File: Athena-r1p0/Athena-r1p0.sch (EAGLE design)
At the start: 86 parts, among them J1 MF-CON-MICROUSB-RIGHT, J3 TC2050-IDC-NL, J4 TC2030-IDC-NL, J5 MF-CON-2.54mm-01x14, J6 MF-CON-2.54mm-01x14, SW1 MF-SW-TACT-4.2MM, SW2 MF-SW-TACT-4.2MM, U1 AP2112, U2 RT9080-18GJ5, U3 MCP73831/2, U4 PRTR5V0U2X,215, U5 FE310, U6 32MBit, U7 MK22FN128VLH10, X1 JST 2-Pin, Y1 TSX-3225-16.0000MF18X-AC0, Y2 KX3211A0032.768000

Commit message: Finished updates based on design review feedback.  Added mounting holes and chassis GND.  Converted all passives to 0402.  Renumbered all parts.  Added cover page.  Replaced SiTime oscillator with std footprint 32kHz oscillator.
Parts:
- removed C33, C34: 15pF, MF_Passives:CAPACITOR_NP_0603
- removed C35, C36, C37: 0.1uF, MF_Passives:CAPACITOR_NP_0402
- removed TP1, TP2, TP3, TP4: TEST-POINT3X5, Athena-r0p1:TEST-POINT3X5
- added B0, B1, B2, B3: TPB0,65, Athena-r0p1:TPB0,65
- added C23, C25: 10uF, MF_Passives:CAPACITOR_NP_0402
- added C24, C26, C29: 0.1uF, MF_Passives:CAPACITOR_NP_0402
- added J7, J8: MF-CON-2.54mm-01x06, MF_Connectors:CON_01X06_PTH_2.54MM
- added MGT1, MGT2, MGT3, MGT4: MOUNTING_HOLE, Athena-r0p1:MOUNTING_HOLE
- added R22, R23: 10, MF_Passives:RESISTOR_0402
- C1, C12: device MF_Passives:CAPACITOR_NP_0603 -> MF_Passives:CAPACITOR_NP_0402; MPN (none) -> CL05A106MP8NUB8
- C10, C20: value 10nF -> 0.1uF; device MF_Passives:CAPACITOR_NP_0603 -> MF_Passives:CAPACITOR_NP_0402
- C11, C16, C18: device MF_Passives:CAPACITOR_NP_0603 -> MF_Passives:CAPACITOR_NP_0402
- C13, C22: value 10uF -> 0.1uF
- C14: value 10uF -> DNP
- C15: value 10uF -> 0.01uF
- C17: value DNP -> 10uF; device MF_Passives:CAPACITOR_NP_0603 -> MF_Passives:CAPACITOR_NP_0402; MPN (none) -> CL05A106MP8NUB8
- C19: value 0.1uF -> 10uF; device MF_Passives:CAPACITOR_NP_0603 -> MF_Passives:CAPACITOR_NP_0402; MPN (none) -> CL05A106MP8NUB8
- C21: MPN (none) -> CL05A106MP8NUB8
- C27: value 0.1uF -> 10uF; MPN (none) -> CL05A106MP8NUB8
- C28: value 0.1uF -> 0.01uF
- C3: value 1uF -> 10uF; MPN (none) -> CL05A106MP8NUB8
- C30: value 0.1uF -> 15pF; MPN (none) -> CL05C150JB5NNNC
- C31: value 10uF -> 15pF; device MF_Passives:CAPACITOR_NP_0603 -> MF_Passives:CAPACITOR_NP_0402; MPN (none) -> CL05C150JB5NNNC
- C6: value 10uF -> 1uF; device MF_Passives:CAPACITOR_NP_0603 -> MF_Passives:CAPACITOR_NP_0402
- D1: value MF-LED-0603-GREEN -> MF-LED-0603-RED; device MF_LEDs:LED_SINGLE-0603-GREEN -> MF_LEDs:LED_SINGLE-0603-RED
- D2: value MF-LED-0603-RED -> MF-LED-0603-GREEN; device MF_LEDs:LED_SINGLE-0603-RED -> MF_LEDs:LED_SINGLE-0603-GREEN
- FRAME1: SHEETNM Power (Nest) -> Power
- FRAME2: SHEETNM USB-JTAG (NEST) -> MK22 Controller (Nest)
- FRAME3: SHEETNM OFF-BOARD-DEBUG HEADER -> Bridge and Debug Headers
- FRAME4: SHEETNM Microcontroller (Owl) -> FE310 Microcontroller (Owl)
- FRAME6: SHEETNM Headers (Owl) -> I/O Headers (Owl)
- J2: value (none) -> G800LS588010THR
- J5, J6: value MF-CON-2.54mm-01x14 -> MF-CON-2.54mm-01x08; device MF_Connectors:CON_01X14_PTH_2.54MM -> MF_Connectors:CON_01X08_PTH_2.54MM
- R1: value 100k -> 1k
- R10, R11, R12, R9: value 100k -> 100; device MF_Passives:RESISTOR_0603 -> MF_Passives:RESISTOR_0402
- R13, R14: value 100 -> 100k
- R15: value 100 -> 0
- R16: value 100k -> 1M
- R17: value 1M -> 100k; device MF_Passives:RESISTOR_0603 -> MF_Passives:RESISTOR_0402
- R18: value DNP -> 100k
- R2: value 100k -> 10k
- R20: value 100k -> 10
- R21: value 0 -> 10
- R3, R5: value 1k -> 100k
- R4: value 100k -> 1k; device MF_Passives:RESISTOR_0603 -> MF_Passives:RESISTOR_0402
- R6: value 10k -> DNP
- R8: value 100 -> 100k; device MF_Passives:RESISTOR_0603 -> MF_Passives:RESISTOR_0402
- U1: value AP2112 -> PRTR5V0U2X,215; device Athena-r0p1:AP2112 -> Athena-r0p1:PRTR5V0U2X,215
- U2: value RT9080-18GJ5 -> MCP73831/2; device Athena-r0p1:RT9080-18GJ5 -> Athena-r0p1:MCP73831/2
- U3: value MCP73831/2 -> AP2112; device Athena-r0p1:IC_POWER_LIPO_MCP73831/2 -> Athena-r0p1:AP2112
- U4: value PRTR5V0U2X,215 -> RT9080-18GJ5; device Athena-r0p1:PRTR5V0U2X,215 -> Athena-r0p1:RT9080-18GJ5
- U5: value FE310 -> MK22FN128VLH10; device Athena-r0p1:IC_MCU_SIFIVE_FE310 -> Athena-r0p1:MK22FN128VLH10
- U6: value 32MBit -> FE310; device Athena-r0p1:IC_MEMORY_QSPI32MBIT -> Athena-r0p1:IC_MCU_SIFIVE_FE310
- U7: value MK22FN128VLH10 -> 32MBit; device Athena-r0p1:IC_USB_JTAG_MK22FN128VLH10 -> Athena-r0p1:IC_MEMORY_QSPI32MBIT
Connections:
- removed net BATT_VOLT: J6.PIN4, R19.P$2, R20.P$1
- removed net CS2: J5.PIN8, U5.IO9
- removed net CS3: J5.PIN9, U5.IO10
- removed net IO22: J6.PIN10, U5.IO22
- removed net P35: TP1.1, U7.PTB0/LLWU_P5
- removed net P36: TP2.1, U7.PTB1
- removed net P37: TP3.1, U7.PTB2
- removed net P38: TP4.1, U7.PTB3
- removed net PWM0_0: J6.PIN5, U5.IO0
- removed net PWM0_1: J6.PIN6, U5.IO1
- removed net VOLT_BAT: C1.P$2, C10.P$2, C11.P$2, C12.P$2, C13.P$2, C14.P$2, C15.P$2, C18.P$2, C19.P$2, C2.P$2, C20.P$2, C21.P$2, C22.P$2, C27.P$2, C28.P$2, C3.P$2, C30.P$2, C31.P$2, C32.P$2, C33.P$2, C34.P$2, C35.P$2, C36.P$2, C37.P$2, C4.P$2, C5.P$2, C6.P$2, C7.P$2, C8.P$2, C9.P$2, D4.A, D5.A, J1.GND, J1.SLD, J2.15, J2.16, J3.10, J3.7, J3.8, J3.9, J4.5, R18.P$1, R20.P$2, R21.P$2, R3.P$2, R6.P$1, SW1.P$1, SW1.P$2, SW2.P$1, SW2.P$2, U1.GND, U2.GND, U3.VSS, U4.GND/1, U5.GND, U6.GND, U7.GND, U7.VREFL, U7.VSSA, X1.2, Y1.2, Y1.4, Y2.GND
- new net CGND: J1.SLD, MGT1.P$1, MGT2.P$1, MGT3.P$1, MGT4.P$1, R20.P$1, R21.P$1, R22.P$1, R23.P$1
- new net IO1: J6.PIN2, U6.IO1
- new net IO10: J7.PIN2, U6.IO10
- new net IO9: J7.PIN1, U6.IO9
- new net N$12: B0.TP, U5.PTB0/LLWU_P5
- new net N$13: B1.TP, U5.PTB1
- new net N$14: B2.TP, U5.PTB2
- new net N$15: B3.TP, U5.PTB3
- new net PWM: J6.PIN1, U6.IO0
- net 1.8V: now also C15.P$1, C16.P$1, C17.P$1, C6.P$1, J8.PIN3, R12.P$1, U4.VOUT, U6.VDD_CORE; no longer C10.P$1, C11.P$1, C12.P$1, C5.P$1, R8.P$1, U2.VOUT, U5.VDD_CORE
- net 16MHZ_IN: now also C30.P$1, R16.P$1, U6.XTAL_IN; no longer C33.P$1, R17.P$2, U5.XTAL_IN
- net 16MHZ_OUT: now also C31.P$1, R16.P$2, U6.XTAL_OUT; no longer C34.P$1, R17.P$1, U5.XTAL_OUT
- net 3.3V: now also C10.P$1, C11.P$1, C12.P$1, C20.P$1, C23.P$1, C24.P$1, C25.P$1, C26.P$1, C29.P$1, C5.P$1, D2.ANODE, J5.PIN7, J8.PIN2, R13.P$1, R14.P$1, R17.P$1, R18.P$1, R19.P$1, R6.P$2, R8.P$1, U3.OUT, U4.VIN, U5.PTA4/LLWU_P3, U5.USBVDD, U5.VBATT, U5.VDD, U5.VDDA, U5.VREFH, U6.AON_VDD, U6.AON_VDD_IO, U6.OTP_AIVDD, U6.VDD_IO, U7.VCC; no longer C13.P$1, C14.P$1, C15.P$1, C28.P$1, C3.P$1, C30.P$1, C31.P$1, C35.P$1, C36.P$1, C37.P$1, D1.ANODE, J5.PIN14, J5.PIN2, J6.PIN14, R10.P$1, R11.P$1, R12.P$1, R16.P$1, R4.P$1, R7.P$2, R9.P$1, U1.OUT, U2.VIN, U5.AON_VDD, U5.AON_VDD_IO, U5.OTP_AIVDD, U5.VDD_IO, U6.VCC, U7.PTA4/LLWU_P3, U7.USBVDD, U7.VBATT, U7.VDD, U7.VDDA, U7.VREFH
- net 32KHZ_CLK: now also U6.AON_PSD_LFALTCLK; no longer U5.AON_PSD_LFALTCLK
- net CS0: now also J5.PIN3, U6.IO2; no longer J5.PIN4, U5.IO2
- net DBG_RESET: now also R8.P$2, U5.RESET_B; no longer R16.P$2, U7.RESET_B
- net DBG_SWDCLK: now also U5.PTA0; no longer U7.PTA0
- net DBG_SWDIO: now also U5.PTA3; no longer U7.PTA3
- net DBG_SWO: now also U5.PTA2; no longer U7.PTA2
- net GND: now also C1.P$2, C10.P$2, C11.P$2, C12.P$2, C15.P$2, C16.P$2, C17.P$2, C18.P$2, C19.P$2, C2.P$2, C20.P$2, C21.P$2, C22.P$2, C23.P$2, C24.P$2, C25.P$2, C26.P$2, C27.P$2, C28.P$2, C29.P$2, C3.P$2, C30.P$2, C31.P$2, C32.P$2, C4.P$2, C5.P$2, C6.P$2, C7.P$2, C8.P$2, C9.P$2, D4.A, D5.A, J1.GND, J2.15, J2.16, J3.10, J3.7, J3.8, J3.9, J4.5, J5.PIN8, J6.PIN8, J8.PIN5, J8.PIN6, R15.P$2, R2.P$1, R20.P$2, R21.P$2, R22.P$2, R23.P$2, R4.P$2, R7.P$1, SW1.P$1, SW1.P$2, SW2.P$1, SW2.P$2, U1.GND/1, U2.VSS, U3.GND, U4.GND, U5.GND, U5.VREFL, U5.VSSA, U6.GND, U7.GND, X1.2, Y1.2, Y1.4, Y2.GND; no longer J5.PIN13, J5.PIN3, J6.PIN13
- net IO11: now also J7.PIN3, U6.IO11; no longer J5.PIN10, U5.IO11
- net IO19: now also J7.PIN4, U6.IO19; no longer J6.PIN7, U5.IO19
- net IO20: now also J7.PIN5, U6.IO20; no longer J6.PIN8, U5.IO20
- net IO21: now also J7.PIN6, U6.IO21; no longer J6.PIN9, U5.IO21
- net JTAG_TCK: now also U6.JTAG_TCK; no longer U5.JTAG_TCK
- net JTAG_TCK_NEST: now also R10.P$2; no longer R14.P$2
- net JTAG_TDI: now also U6.JTAG_TDI; no longer U5.JTAG_TDI
- net JTAG_TDI_NEST: now also R9.P$2; no longer R13.P$2
- net JTAG_TDO: now also U6.JTAG_TDO; no longer U5.JTAG_TDO
- net JTAG_TDO_NEST: now also U5.PTE1/LLWU_P0; no longer U7.PTE1/LLWU_P0
- net JTAG_TMS: now also U6.JTAG_TMS; no longer U5.JTAG_TMS
- net JTAG_TMS_NEST: now also R11.P$1; no longer R15.P$1
- net MISO: now also J5.PIN5, U6.IO4; no longer J5.PIN6, U5.IO4
- net MOSI: now also J5.PIN6, U6.IO3; no longer J5.PIN5, U5.IO3
- net N$1: now also R3.P$1, U3.EN; no longer R1.P$1, U1.EN
- net N$10: now also C13.P$2, C14.P$2, U6.PLL_AVSS; no longer C16.P$2, C17.P$2, U5.PLL_AVSS
- net N$11: now also R9.P$1, U5.PTD2/LLWU_P13; no longer R15.P$2, U7.PTD6/LLWU_P15
- net N$2: now also D2.CATHODE, R4.P$1; no longer D1.CATHODE, R3.P$1
- net N$3: now also D1.CATHODE, R1.P$1; no longer D2.CATHODE, R5.P$1
- net N$4: now also R5.P$2, R6.P$1, R7.P$2, U4.EN; no longer R18.P$2, R2.P$2, R7.P$1, U2.EN
- net N$5: now also R2.P$2, U2.PROG; no longer R6.P$2, U3.PROG
- net N$6: now also R1.P$2, U2.STAT; no longer R5.P$2, U3.STAT
- net N$7: now also R15.P$1, U6.AON_PSD_LFCLKSEL; no longer R21.P$1, U5.AON_PSD_LFCLKSEL
- net N$8: now also R11.P$2, U5.PTD6/LLWU_P15; no longer R13.P$1, U7.PTD2/LLWU_P13
- net N$9: now also R10.P$1, U5.PTD5; no longer R14.P$1, U7.PTD5
- net PLL_AVDD: now also C13.P$1, C14.P$1, R12.P$2, U6.PLL_AVDD; no longer C16.P$1, C17.P$1, R8.P$2, U5.PLL_AVDD
- net QSPI_CS: now also R19.P$2, U6.QSPI_CS, U7.CE#; no longer R10.P$2, U5.QSPI_CS, U6.CE#
- net QSPI_DQ0: now also U6.QSPI_DQ_0, U7.MOSI/IO0; no longer U5.QSPI_DQ_0, U6.MOSI/IO0
- net QSPI_DQ1: now also U6.QSPI_DQ_1, U7.MISO/IO1; no longer U5.QSPI_DQ_1, U6.MISO/IO1
- net QSPI_DQ2: now also R17.P$2, U6.QSPI_DQ_2, U7.WP#/IO2; no longer R4.P$2, U5.QSPI_DQ_2, U6.WP#/IO2
- net QSPI_DQ3: now also R18.P$2, U6.QSPI_DQ_3, U7.HOLD#/IO3; no longer R9.P$2, U5.QSPI_DQ_3, U6.HOLD#/IO3
- net QSPI_SCK: now also U6.QSPI_SCK, U7.SCK; no longer U5.QSPI_SCK, U6.SCK
- net RESET: now also C28.P$1, J5.PIN2, R14.P$2, U6.AON_ERST_N; no longer C20.P$1, J6.PIN1, R12.P$2, U5.AON_ERST_N
- net RESET_NEST: now also U5.PTD7; no longer U7.PTD7
- net RXI: now also J6.PIN3, U6.IO23; no longer J6.PIN12, U5.IO23
- net SCK: now also J5.PIN4, U6.IO5; no longer J5.PIN7, U5.IO5
- net SCL: now also J6.PIN5, U6.IO13; no longer J5.PIN12, U5.IO13
- net SDA: now also J6.PIN6, U6.IO12; no longer J5.PIN11, U5.IO12
- net TXO: now also J6.PIN4, U6.IO18; no longer J6.PIN11, U5.IO18
- net UART_RX: now also U6.IO16; no longer U5.IO16
- net UART_RX_NEST: now also U5.PTB16; no longer U7.PTB16
- net UART_TX: now also U6.IO17; no longer U5.IO17
- net UART_TX_NEST: now also U5.PTB17; no longer U7.PTB17
- net USB_N: now also U1.3, U5.D-; no longer U4.3, U7.D-
- net USB_P: now also U1.2, U5.D+; no longer U4.2, U7.D+
- net VDD_CORE_EN: now also J8.PIN4, R5.P$1, U6.AON_PMU_OUT_0; no longer J6.PIN3, R2.P$1, U5.AON_PMU_OUT_0
- net V_BATT: now also C1.P$1, U2.VBAT; no longer C6.P$1, R19.P$1, U3.VBAT
- net V_USB: now also C3.P$1, D1.ANODE, J6.PIN7, J8.PIN1, R3.P$2, U1.VDD/4, U2.VDD, U3.IN; no longer C1.P$1, D2.ANODE, J5.PIN1, R1.P$2, U1.IN, U3.VDD, U4.VDD/4
- net WAKE: now also J5.PIN1, R13.P$2, U6.AON_DWAKEUP_N; no longer J6.PIN2, R11.P$2, U5.AON_DWAKEUP_N
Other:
- note added: "1"
- note added: "2"
- note added: "3"
- note added: "4"
- note added: "5"
- note added: "6"
- note added: "7"
- note added: "Athena Design Rev. 1.0 Schematic"
- note added: "Aug. 5, 2021"
- note added: "Cover Page"
- note added: "Debug Control: MK22 Processor"
- note added: "Debug Headers: MK22 Tag, FE310 Tag, MK22->FE310 Bridge"
- note added: "Description"
- note added: "Designed in EAGLE 9.6.2."
- note added: "GPIO Header"
- note added: "I/O Headers: mikroBus-Compatible, GPIO, and Power; Mechanical"
- note added: "J2 Bridge connector notes Default: Closed (1->2, 3->4, ..., 15->16) to program/debug on-board (Athena) FE310. Open and access NEST-side pins to program/debug off-board FE310 using Athena MK22 controller."
- note added: "Main Processor: SiFive FE310, the RISC-V MCU"
- note added: "Mechanical & Grounds"
- note added: "Peripherals: Oscillators, Flash Memory"
- note added: "Power Header"
- note added: "Power: USB, Charging, Voltage Regulators"
- note added: "RVR Lab, Rice University, Houston TX"
- note added: "Sheet"
- note added: "The first RISC-V development board at Rice University, featuring the SiFive FE310 microprocessor, Athena is a prototyping and experimental platform for education and research at Rice. It is intended to be used in undergraduate lab courses and in VIP projects, therefore the design focus is on debug capability and I/O access."
- note added: "mikroBus Left Header"
- note added: "mikroBus Right Header"
- note removed: "CONTROL"
- note removed: "GPIO"
- note removed: "I2C"
- note removed: "J1 Bridge connector notes Default: Closed (1->2, 3->4, ..., 15->16) to program/debug on-board (Athena) FE310. Open and access NEST-side pins to program/debug off-board FE310 using Athena MK22 controller."
- note removed: "POWER"
- note removed: "SPI1"
- note removed: "UART1"

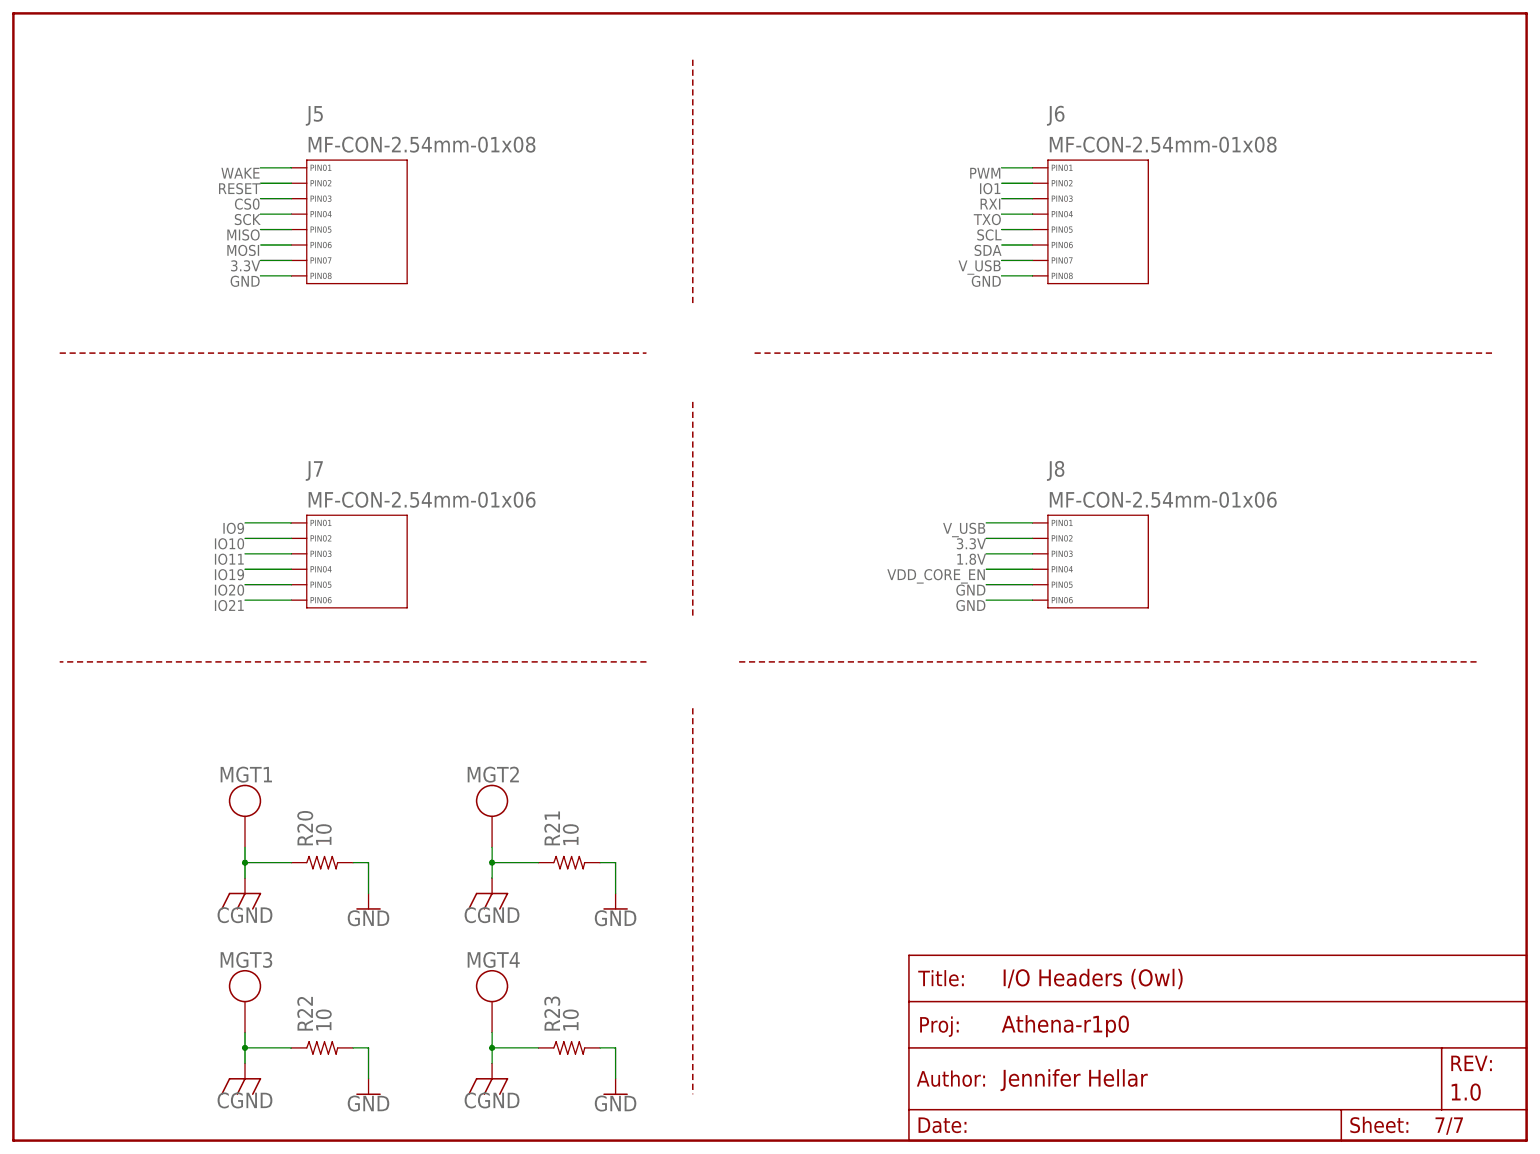
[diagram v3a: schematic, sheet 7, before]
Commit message: First pass at Athena layout.  Passes all DRC except for issues with the USB port pads (which is a MF housepart)
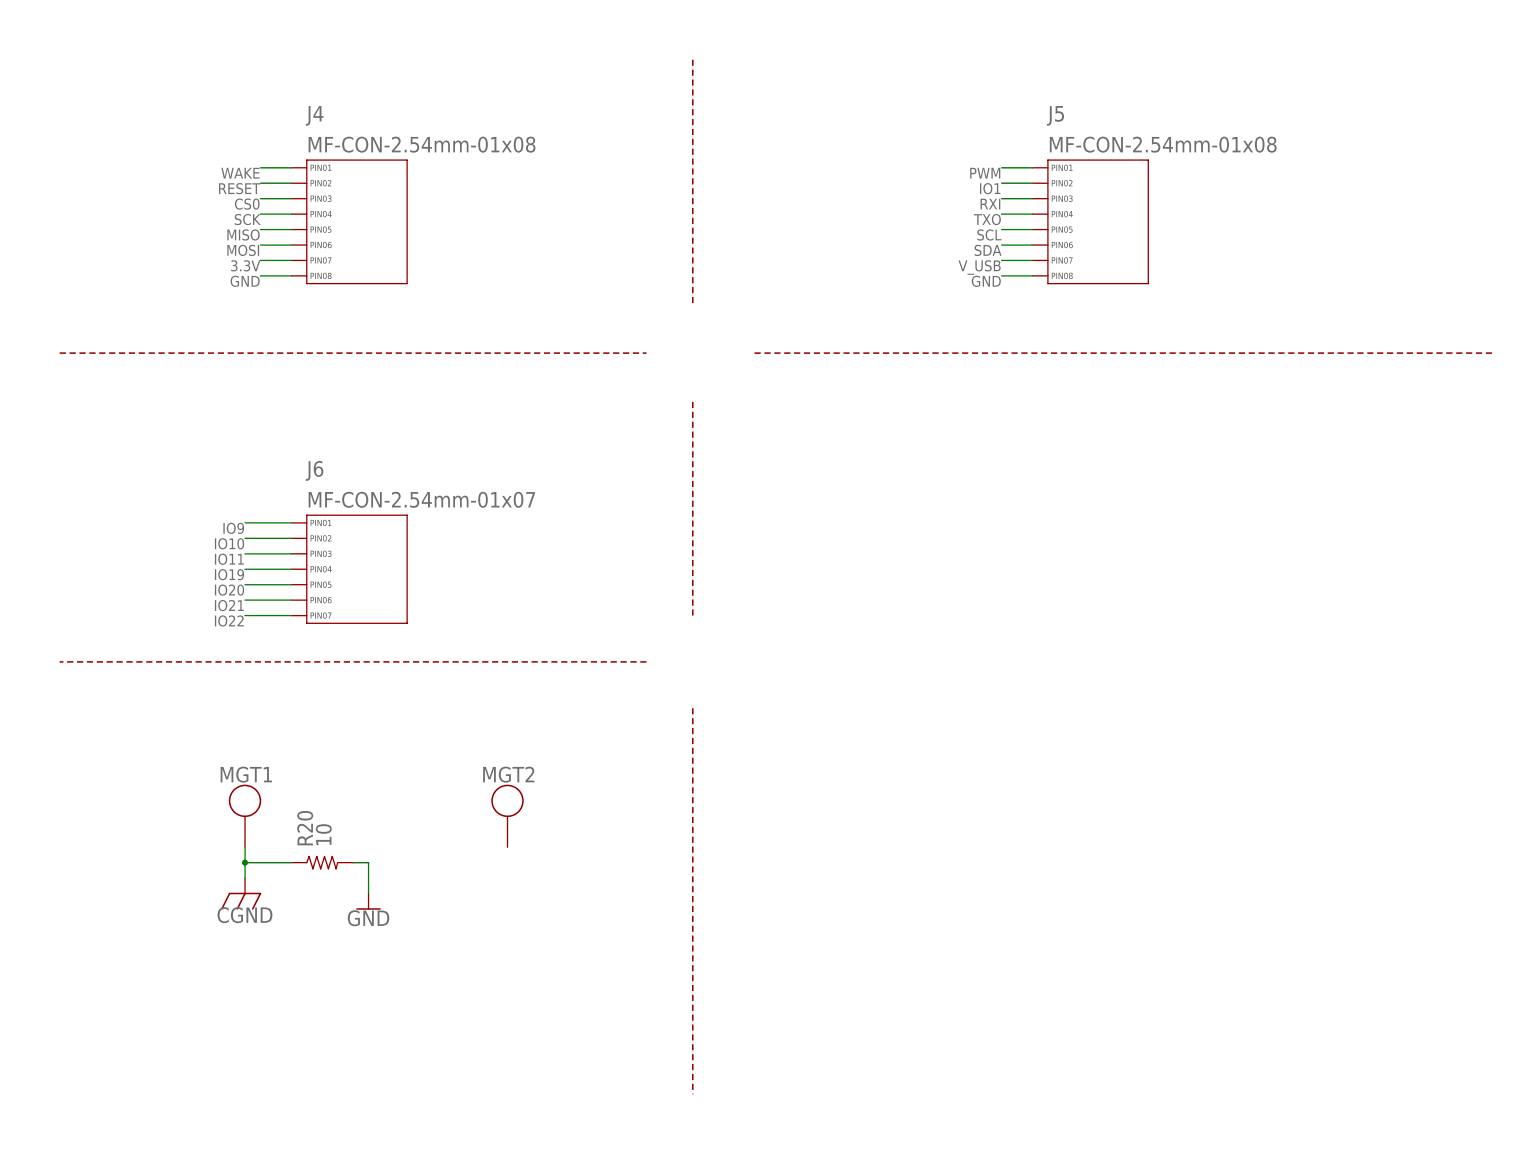
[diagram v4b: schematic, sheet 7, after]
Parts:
- removed FRAME1, FRAME2, FRAME3, FRAME4, FRAME5, FRAME6: FRAME-LETTER, Athena-r0p1:FRAME-LETTER
- removed J7, J8: MF-CON-2.54mm-01x06, MF_Connectors:CON_01X06_PTH_2.54MM
- removed MGT3, MGT4: MOUNTING_HOLE, Athena-r0p1:MOUNTING_HOLE
- removed R21, R22, R23: 10, MF_Passives:RESISTOR_0402
- B0, B1, B2, B3: device Athena-r0p1:TPB0,65 -> Athena-r1p0:TPB0,65
- C1, C10, C11, C12, C13, C14, C15, C16, C17, C18, C19, C2, C20, C21, C22, C23, C24, C25, C26, C27, C28, C29, C3, C30, C31, C32, C4, C5, C6, C7, C8, C9: device MF_Passives:CAPACITOR_NP_0402 -> Athena-r1p0:CAPACITOR_NP_0402
- D1: value MF-LED-0603-RED -> MF-LED-0805-RED; device MF_LEDs:LED_SINGLE-0603-RED -> Athena-r1p0:LED_SINGLE-0603-RED
- D2: device MF_LEDs:LED_SINGLE-0603-GREEN -> Athena-r1p0:LED_SINGLE-0603-GREEN
- D3: device Athena-r0p1:DIODE-SCHOTTKYSOD-123 -> Athena-r1p0:DIODE-SCHOTTKYSOD-123
- D4, D5: device Athena-r0p1:PESD0603-240TVS0603 -> Athena-r1p0:PESD0603-240TVS0603
- J1: device MF_Connectors:USB_MICRO_RIGHT -> Athena-r1p0:USB_MICRO_RIGHT
- J2: device SparkFun-Connectors:CONN_08X2 -> Athena-r1p0:CONN_08X2
- J3: value TC2050-IDC-NL -> TC2030-IDC-NL; device Athena-r0p1:TC2050-IDC-NL -> Athena-r1p0:TC2030-IDC-NL
- J4: value TC2030-IDC-NL -> MF-CON-2.54mm-01x08; device Athena-r0p1:TC2030-IDC-NL -> Athena-r1p0:CON_01X08_PTH_2.54MM
- J5: device MF_Connectors:CON_01X08_PTH_2.54MM -> Athena-r1p0:CON_01X08_PTH_2.54MM
- J6: value MF-CON-2.54mm-01x08 -> MF-CON-2.54mm-01x07; device MF_Connectors:CON_01X08_PTH_2.54MM -> Athena-r1p0:CON_01X07_PTH_2.54MM
- MGT1, MGT2: device Athena-r0p1:MOUNTING_HOLE -> Athena-r1p0:MOUNTING_HOLE
- R1, R10, R11, R12, R13, R14, R15, R16, R17, R18, R19, R2, R20, R3, R4, R5, R6, R7, R8, R9: device MF_Passives:RESISTOR_0402 -> Athena-r1p0:RESISTOR_0402
- SW1, SW2: value MF-SW-TACT-4.2MM -> MF-SW-TACT-6MM; device MF_Switches:TACT_4.2MM -> Athena-r1p0:TACT_4.2MM
- U1: device Athena-r0p1:PRTR5V0U2X,215 -> Athena-r1p0:PRTR5V0U2X,215
- U2: device Athena-r0p1:MCP73831/2 -> Athena-r1p0:MCP73831/2
- U3: device Athena-r0p1:AP2112 -> Athena-r1p0:AP2112
- U4: device Athena-r0p1:RT9080-18GJ5 -> Athena-r1p0:RT9080-18GJ5
- U5: device Athena-r0p1:MK22FN128VLH10 -> Athena-r1p0:MK22FN128VLH10
- U6: device Athena-r0p1:IC_MCU_SIFIVE_FE310 -> Athena-r1p0:IC_MCU_SIFIVE_FE310
- U7: device Athena-r0p1:IC_MEMORY_QSPI32MBIT -> Athena-r1p0:IC_MEMORY_QSPI32MBIT
- X1: device Athena-r0p1:CONNECTORS_BATT_JST_PH_2PIN -> Athena-r1p0:CONNECTORS_BATT_JST_PH_2PIN
- Y1: device Athena-r0p1:TSX-3225-16.0000MF18X-AC0 -> Athena-r1p0:TSX-3225-16.0000MF18X-AC0
- Y2: device Athena-r0p1:KX3211A0032.768000 -> Athena-r1p0:KX3211A0032.768000
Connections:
- new net IO22: J6.PIN7, U6.IO22
- net 1.8V: no longer J8.PIN3
- net 3.3V: now also J3.1, J4.PIN7; no longer J3.6, J4.1, J5.PIN7, J8.PIN2
- net CGND: no longer MGT2.P$1, MGT3.P$1, MGT4.P$1, R21.P$1, R22.P$1, R23.P$1
- net CS0: now also J4.PIN3; no longer J5.PIN3
- net DBG_RESET: now also J3.3; no longer J4.3
- net DBG_SWDCLK: now also J3.4; no longer J4.4
- net DBG_SWDIO: now also J3.2; no longer J4.2
- net DBG_SWO: now also J3.6; no longer J4.6
- net GND: now also J3.5, J4.PIN8; no longer J3.10, J3.7, J3.8, J3.9, J4.5, J6.PIN8, J8.PIN5, J8.PIN6, R21.P$2, R22.P$2, R23.P$2
- net IO1: now also J5.PIN2; no longer J6.PIN2
- net IO10: now also J6.PIN2; no longer J7.PIN2
- net IO11: now also J6.PIN3; no longer J7.PIN3
- net IO19: now also J6.PIN4; no longer J7.PIN4
- net IO20: now also J6.PIN5; no longer J7.PIN5
- net IO21: now also J6.PIN6; no longer J7.PIN6
- net IO9: now also J6.PIN1; no longer J7.PIN1
- net JTAG_TCK: no longer J3.4
- net JTAG_TDI: no longer J3.2
- net JTAG_TDO: no longer J3.3
- net JTAG_TMS: no longer J3.5
- net MISO: now also J4.PIN5; no longer J5.PIN5
- net MOSI: now also J4.PIN6; no longer J5.PIN6
- net PWM: now also J5.PIN1; no longer J6.PIN1
- net RESET: now also J4.PIN2; no longer J3.1, J5.PIN2
- net RXI: now also J5.PIN3; no longer J6.PIN3
- net SCK: now also J4.PIN4; no longer J5.PIN4
- net SCL: now also J5.PIN5; no longer J6.PIN5
- net SDA: now also J5.PIN6; no longer J6.PIN6
- net TXO: now also J5.PIN4; no longer J6.PIN4
- net USB_N: now also U1.2; no longer U1.3
- net USB_P: now also U1.3; no longer U1.2
- net VDD_CORE_EN: no longer J8.PIN4
- net V_USB: now also J5.PIN7; no longer J6.PIN7, J8.PIN1
- net WAKE: now also J4.PIN1; no longer J5.PIN1
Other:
- note removed: "Power Header"
- moved on the sheet: J5, MGT2

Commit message: Updated design
Removed off-board debug header
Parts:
- removed J6: MF-CON-2.54mm-01x07, Athena-r1p0:CON_01X07_PTH_2.54MM
- J2: value G800LS588010THR -> TC2030-IDC-NL; device Athena-r1p0:CONN_08X2 -> Athena-r1p0:TC2030-IDC-NL
- J3: value TC2030-IDC-NL -> MF-CON-2.54mm-01x08; device Athena-r1p0:TC2030-IDC-NL -> Athena-r1p0:CON_01X08_PTH_2.54MM
- J5: value MF-CON-2.54mm-01x08 -> MF-CON-2.54mm-01x07; device Athena-r1p0:CON_01X08_PTH_2.54MM -> Athena-r1p0:CON_01X07_PTH_2.54MM
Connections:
- removed net JTAG_TCK_NEST: J2.8, R10.P$2
- removed net JTAG_TDI_NEST: J2.12, R9.P$2
- removed net JTAG_TDO_NEST: J2.10, U5.PTE1/LLWU_P0
- removed net JTAG_TMS_NEST: J2.6, R11.P$1
- removed net RESET_NEST: J2.14, U5.PTD7
- removed net UART_RX: J2.3, U6.IO16
- removed net UART_RX_NEST: J2.2, U5.PTB16
- removed net UART_TX: J2.1, U6.IO17
- removed net UART_TX_NEST: J2.4, U5.PTB17
- new net UART_RX_MK22: U5.PTB16, U6.IO17
- new net UART_TX_MK22: U5.PTB17, U6.IO16
- net 3.3V: now also J2.1, J3.PIN7; no longer J3.1, J4.PIN7
- net CS0: now also J3.PIN3; no longer J4.PIN3
- net DBG_RESET: now also J2.3; no longer J3.3
- net DBG_SWDCLK: now also J2.4; no longer J3.4
- net DBG_SWDIO: now also J2.2; no longer J3.2
- net DBG_SWO: now also J2.6; no longer J3.6
- net GND: now also J2.5, J3.PIN8, MGT2.P$1; no longer J2.15, J2.16, J3.5, J5.PIN8
- net IO1: now also J4.PIN2; no longer J5.PIN2
- net IO10: now also J5.PIN2; no longer J6.PIN2
- net IO11: now also J5.PIN3; no longer J6.PIN3
- net IO19: now also J5.PIN4; no longer J6.PIN4
- net IO20: now also J5.PIN5; no longer J6.PIN5
- net IO21: now also J5.PIN6; no longer J6.PIN6
- net IO22: now also J5.PIN7; no longer J6.PIN7
- net IO9: now also J5.PIN1; no longer J6.PIN1
- net JTAG_TCK: now also R10.P$2; no longer J2.7
- net JTAG_TDI: now also R9.P$2; no longer J2.11
- net JTAG_TDO: now also U5.PTE1/LLWU_P0; no longer J2.9
- net JTAG_TMS: now also R11.P$1; no longer J2.5
- net MISO: now also J3.PIN5; no longer J4.PIN5
- net MOSI: now also J3.PIN6; no longer J4.PIN6
- net PWM: now also J4.PIN1; no longer J5.PIN1
- net RESET: now also J3.PIN2, U5.PTD7; no longer J2.13, J4.PIN2
- net RXI: now also J4.PIN3; no longer J5.PIN3
- net SCK: now also J3.PIN4; no longer J4.PIN4
- net SCL: now also J4.PIN5; no longer J5.PIN5
- net SDA: now also J4.PIN6; no longer J5.PIN6
- net TXO: now also J4.PIN4; no longer J5.PIN4
- net V_USB: now also J4.PIN7; no longer J5.PIN7
- net WAKE: now also J3.PIN1; no longer J4.PIN1
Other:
- note added: "J2 6pin Tag-Connect, MK22 Debug"
- note added: "May 18, 2022"
- note added: "RX/TX labels match MK22 datasheet"
- note added: "RX/TX_MK22 labels consistent with MK22 datasheet"
- note removed: "7"
- note removed: "Aug. 5, 2021"
- note removed: "Debug Headers: MK22 Tag, FE310 Tag, MK22->FE310 Bridge"
- note removed: "J2 Bridge connector notes Default: Closed (1->2, 3->4, ..., 15->16) to program/debug on-board (Athena) FE310. Open and access NEST-side pins to program/debug off-board FE310 using Athena MK22 controller."
- note removed: "J2 Bridge for on/off-board FE310 Debug, J3 10pin Tag-Connect for on-board FE310 Debug"
- note removed: "J4 6pin Tag-Connect, MK22 Debug"
- note removed: "RX/TX labels corr. to FE310 persp."
- note removed: "RX/TX labels match FE310 datasheet"
- note removed: "RX/TX_NEST labels consistent with MK22 datasheet"
- note removed: "RX/TX_NEST labels corr. to MK22 persp."
